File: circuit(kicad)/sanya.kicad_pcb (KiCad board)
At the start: 2 copper layers, 34.4 x 27.8 mm, 10 parts, among them J1 Oled, J2 Micro_SD_Card, SW1 Up, SW2 Down, SW3 Set, SW4 SW_DPDT_x2, U1 ATmega328P-A

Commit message: подвигал дорожки, добавил лого :)
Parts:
- moved J2 12.0 mm to (153.3, 68.4), turned to -90 degrees
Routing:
- net VCC: track 87.4 -> 67.8 mm
- net /SCL: track 0.00 -> 10.4 mm
- net /SDA: track 0.00 -> 9.48 mm
- net unconnected-(U1-XTAL2/PB7-Pad8): track 3.89 -> 0.00 mm
- net /PD4: track 33.2 -> 35.8 mm
- net /PD6: track 14.5 -> 16.6 mm
- net Earth: track 115.2 -> 116.3 mm
- net /MOSI: track 9.72 -> 8.69 mm
- net /MISO: track 17.1 -> 16.4 mm

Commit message: v 1.0: Release
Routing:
- net /PD4: track 35.8 -> 34.7 mm
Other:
- board size 34.4 x 27.8 mm -> 37.2 x 30.5 mm

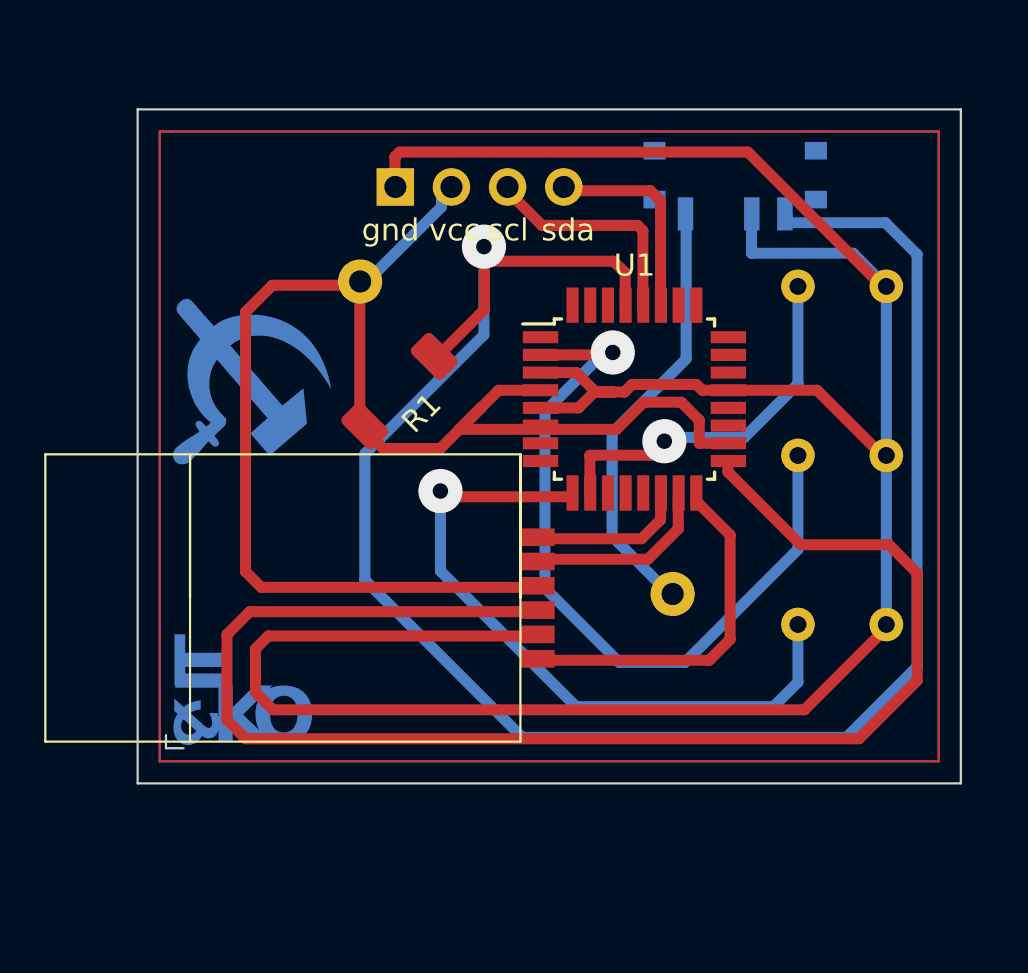
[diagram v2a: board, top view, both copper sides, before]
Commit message: Убрал ненужные контактные площадки, увеличил размеры площадок под кнопки, убрал переходное под МК
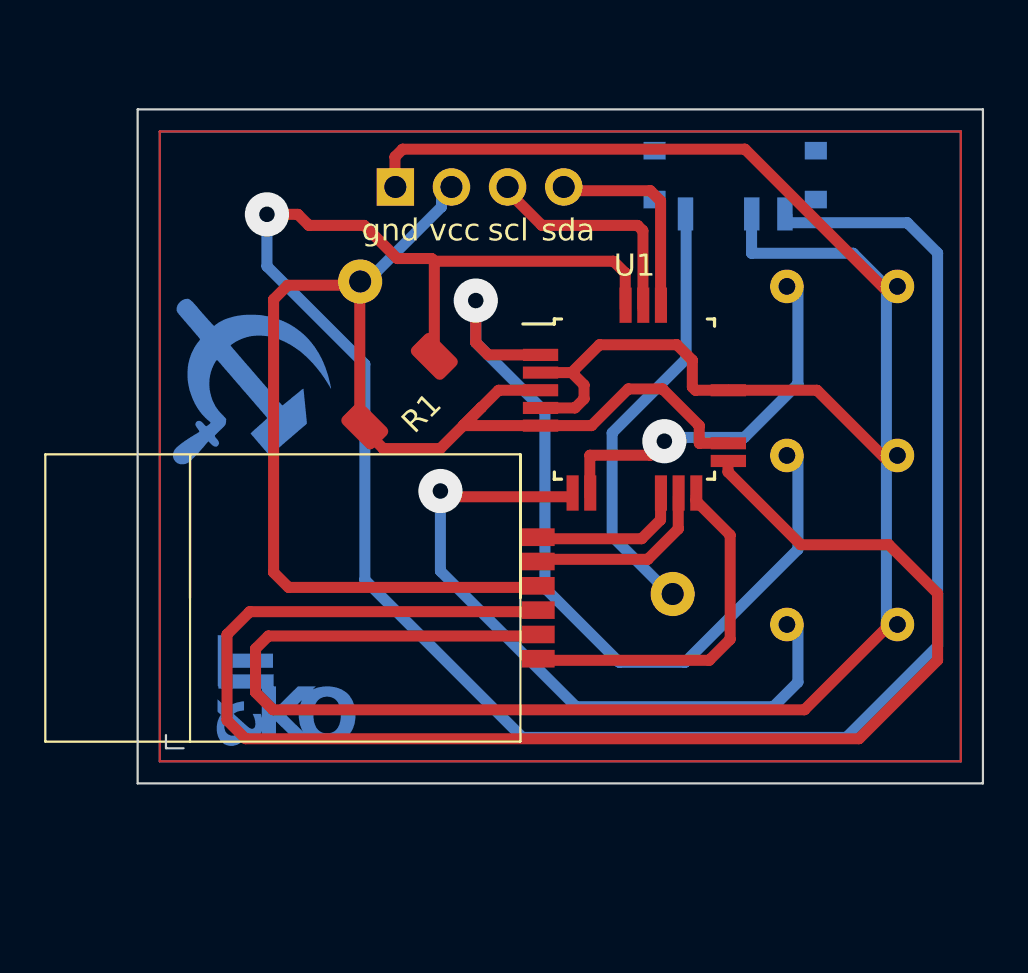
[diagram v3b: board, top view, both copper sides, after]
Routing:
- net /RST: track 85.7 -> 97.7 mm
- net /PD4: track 34.7 -> 39.0 mm
- net VCC: track 68.1 -> 65.8 mm
- net Earth: track 116.5 -> 118.0 mm
- net /SCK: track 66.4 -> 67.2 mm
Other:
- board size 37.2 x 30.5 mm -> 38.2 x 30.5 mm

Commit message: Сделал перемычку м/у RST и GND
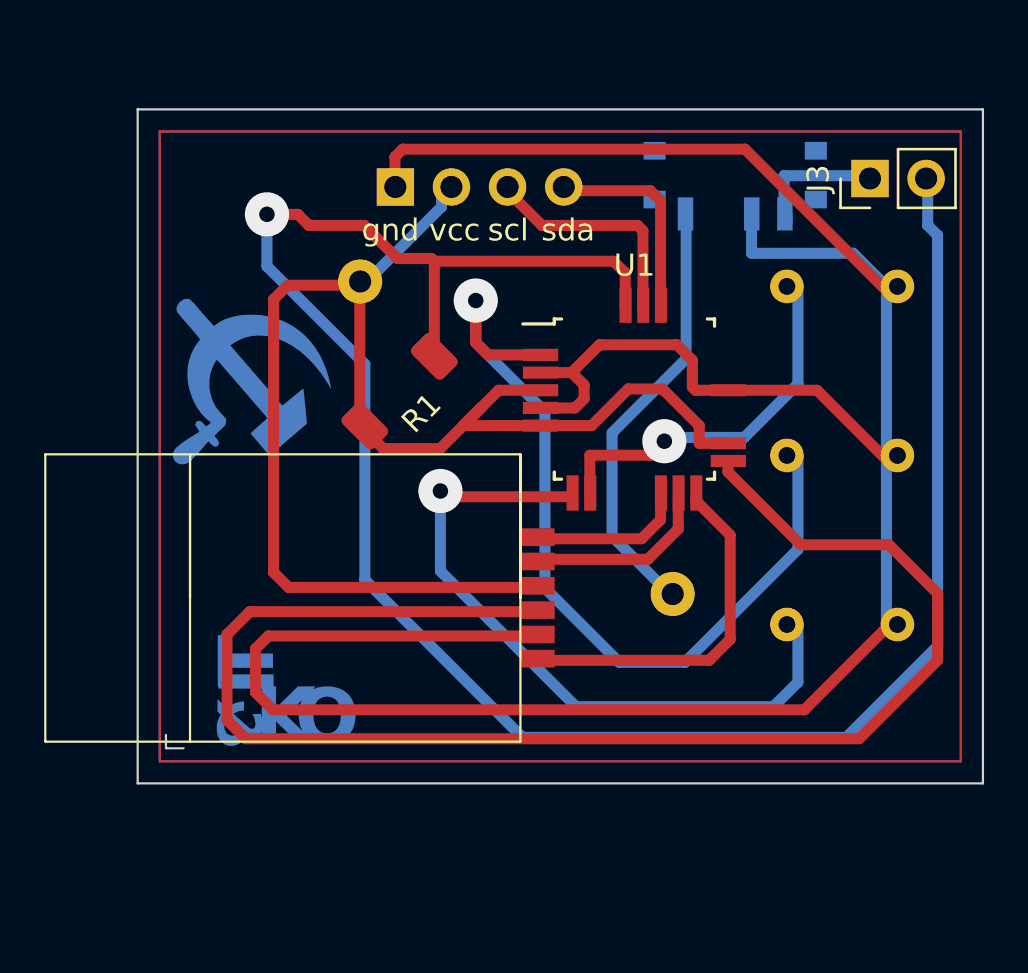
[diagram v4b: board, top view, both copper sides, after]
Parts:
- added J3: sw1, Connector_PinHeader_2.54mm:PinHeader_1x02_P2.54mm_Vertical, F.Cu at (169.1, 49.4)
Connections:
- SW4 pad 3: /RST -> Net-(J3-Pin_1)
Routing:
- net Net-(J3-Pin_1): track 0.00 -> 6.04 mm
- net /RST: track 97.7 -> 93.6 mm
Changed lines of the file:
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@@
   (net 12 "/PD4")
   (net 13 "Net-(BT1--)")
+  (net 14 "Net-(J3-Pin_1)")
   (footprint "Library:Button" (layer "F.Cu")
     (at 167.88 69.56)
@@
       (net 1 "Earth") (pinfunction "2") (pintype "passive"))
   )
+  (footprint "Connector_PinHeader_2.54mm:PinHeader_1x02_P2.54mm_Vertical" (layer "F.Cu")
+    (at 169.1386 49.3776 90)
+    (descr "Through hole straight pin header, 1x02, 2.54mm pitch, single row")
+    (tags "Through hole pin header THT 1x02 2.54mm single row")
+    (property "Sheetfile" "sanya.kicad_sch")
+    (property "Sheetname" "")
+    (property "ki_description" "Generic connector, single row, 01x02, script generated")
+    (property "ki_keywords" "connector")
+    (attr through_hole)
+    (fp_text reference "J3" (at 0 -2.33 90) (layer "F.SilkS")
+        (effects (font (size 1 1) (thickness 0.15)))
+    )
+    (fp_text value "sw1" (at 0 4.87 90) (layer "F.Fab")
+        (effects (font (size 1 1) (thickness 0.15)))
+    )
+    (fp_text user "${REFERENCE}" (at 0 1.27) (layer "F.Fab")
+        (effects (font (size 1 1) (thickness 0.15)))
+    )
+    (fp_line (start -1.33 -1.33) (end 0 -1.33)
+      (stroke (width 0.12) (type solid)) (layer "F.SilkS"))
+    (fp_line (start -1.33 0) (end -1.33 -1.33)
+      (stroke (width 0.12) (type solid)) (layer "F.SilkS"))
+    (fp_line (start -1.33 1.27) (end -1.33 3.87)
+      (stroke (width 0.12) (type solid)) (layer "F.SilkS"))
+    (fp_line (start -1.33 1.27) (end 1.33 1.27)
+      (stroke (width 0.12) (type solid)) (layer "F.SilkS"))
+    (fp_line (start -1.33 3.87) (end 1.33 3.87)
+      (stroke (width 0.12) (type solid)) (layer "F.SilkS"))
+    (fp_line (start 1.33 1.27) (end 1.33 3.87)
+      (stroke (width 0.12) (type solid)) (layer "F.SilkS"))
+    (fp_line (start -1.5 -1.5) (end -1.5 4)
+      (stroke (width 0.05) (type default)) (layer "F.CrtYd"))
+    (fp_line (start 1.5 -1.5) (end -1.5 -1.5)
+      (stroke (width 0.05) (type default)) (layer "F.CrtYd"))
+    (fp_line (start 1.5 4) (end -1.5 4)
+      (stroke (width 0.05) (type default)) (layer "F.CrtYd"))
+    (fp_line (start 1.5 4) (end 1.5 -1.5)
+      (stroke (width 0.05) (type default)) (layer "F.CrtYd"))
+    (fp_line (start -1.27 -0.635) (end -0.635 -1.27)
+      (stroke (width 0.1) (type solid)) (layer "F.Fab"))
+    (fp_line (start -1.27 3.81) (end -1.27 -0.635)
+      (stroke (width 0.1) (type solid)) (layer "F.Fab"))
+    (fp_line (start -0.635 -1.27) (end 1.27 -1.27)
+      (stroke (width 0.1) (type solid)) (layer "F.Fab"))
+    (fp_line (start 1.27 -1.27) (end 1.27 3.81)
+      (stroke (width 0.1) (type solid)) (layer "F.Fab"))
+    (fp_line (start 1.27 3.81) (end -1.27 3.81)
+      (stroke (width 0.1) (type solid)) (layer "F.Fab"))
+    (pad "1" thru_hole rect (at 0 0 90) (size 1.7 1.7) (drill 1) (layers "*.Cu" "*.Mask")
+      (net 14 "Net-(J3-Pin_1)") (pinfunction "Pin_1") (pintype "passive"))
+    (pad "2" thru_hole oval (at 0 2.54 90) (size 1.7 1.7) (drill 1) (layers "*.Cu" "*.Mask")
+      (net 9 "/RST") (pinfunction "Pin_2") (pintype "passive"))
+    (model "${KICAD6_3DMODEL_DIR}/Connector_PinHeader_2.54mm.3dshapes/PinHeader_1x02_P2.54mm_Vertical.wrl"
+      (offset (xyz 0 0 0))
+      (scale (xyz 1 1 1))
+      (rotate (xyz 0 0 0))
+    )
+  )
   (footprint "Connector_Card:microSD_HC_Wuerth_693072010801" (layer "F.Cu")
     (at 153.32 68.36 -90)
@@
       (net 1 "Earth") (pinfunction "B") (pintype "passive"))
     (pad "3" smd rect (at 2.25 1.43) (size 0.7 1.5) (layers "B.Cu" "B.Paste" "B.Mask")
-      (net 9 "/RST") (pinfunction "C") (pintype "passive"))
+      (net 14 "Net-(J3-Pin_1)") (pinfunction "C") (pintype "passive"))
     (model "${KICAD6_3DMODEL_DIR}/Button_Switch_SMD.3dshapes/SW_SPDT_PCM12.wrl"
       (offset (xyz 0 0 0))
@@
   (segment (start 149.423313 53.1203) (end 149.423313 57.426687) (width 0.5) (layer "F.Cu") (net 9))
   (via (at 141.85 51) (size 2) (drill 0.7) (layers "F.Cu" "B.Cu") (net 9))
-  (segment (start 146.28 67.54) (end 153.41 74.67) (width 0.5) (layer "B.Cu") (net 9))
-  (segment (start 170.83 51.38) (end 165.38 51.38) (width 0.5) (layer "B.Cu") (net 9))
-  (segment (start 165.38 51.38) (end 165.38 51.03) (width 0.5) (layer "B.Cu") (net 9))
-  (segment (start 141.85 53.35) (end 146.28 57.78) (width 0.5) (layer "B.Cu") (net 9))
-  (segment (start 172.2 70.54) (end 172.2 52.75) (width 0.5) (layer "B.Cu") (net 9))
-  (segment (start 153.41 74.67) (end 168.07 74.67) (width 0.5) (layer "B.Cu") (net 9))
-  (segment (start 172.2 52.75) (end 170.83 51.38) (width 0.5) (layer "B.Cu") (net 9))
-  (segment (start 168.07 74.67) (end 172.2 70.54) (width 0.5) (layer "B.Cu") (net 9))
-  (segment (start 141.85 51) (end 141.85 53.35) (width 0.5) (layer "B.Cu") (net 9))
-  (segment (start 146.28 57.78) (end 146.28 67.54) (width 0.5) (layer "B.Cu") (net 9))
+  (segment (start 146.28 57.78) (end 141.85 53.35) (width 0.5) (layer "B.Cu") (net 9))
+  (segment (start 153.41 74.67) (end 146.28 67.54) (width 0.5) (layer "B.Cu") (net 9))
+  (segment (start 171.75 49.449) (end 171.75 51.5) (width 0.5) (layer "B.Cu") (net 9))
+  (segment (start 171.6786 49.3776) (end 171.75 49.449) (width 0.5) (layer "B.Cu") (net 9))
+  (segment (start 171.75 51.5) (end 172.2 51.95) (width 0.5) (layer "B.Cu") (net 9))
+  (segment (start 168.07 74.67) (end 153.41 74.67) (width 0.5) (layer "B.Cu") (net 9))
+  (segment (start 146.28 67.54) (end 146.28 57.78) (width 0.5) (layer "B.Cu") (net 9))
+  (segment (start 172.2 51.95) (end 172.2 70.54) (width 0.5) (layer "B.Cu") (net 9))
+  (segment (start 172.2 70.54) (end 168.07 74.67) (width 0.5) (layer "B.Cu") (net 9))
+  (segment (start 141.85 53.35) (end 141.85 51) (width 0.5) (layer "B.Cu") (net 9))
   (segment (start 156.4633 63.7803) (end 156.4633 61.9) (width 0.5) (layer "F.Cu") (net 10))
   (segment (start 156.4633 61.9) (end 159.1998 61.9) (width 0.5) (layer "F.Cu") (net 10))
@@
   (segment (start 160.82 51.01) (end 160.82 57.54) (width 0.5) (layer "B.Cu") (net 13))
   (segment (start 160.82 57.54) (end 157.47 60.89) (width 0.5) (layer "B.Cu") (net 13))
+  (segment (start 165.38 51.38) (end 165.38 51.03) (width 0.5) (layer "B.Cu") (net 14))
+  (segment (start 169.1386 49.3776) (end 169.011 49.25) (width 0.5) (layer "B.Cu") (net 14))
+  (segment (start 165.25 49.25) (end 165.25 50.94) (width 0.5) (layer "B.Cu") (net 14))
+  (segment (start 169.011 49.25) (end 165.25 49.25) (width 0.5) (layer "B.Cu") (net 14))
+  (segment (start 165.25 50.94) (end 165.29 50.98) (width 0.5) (layer "B.Cu") (net 14))
 )
